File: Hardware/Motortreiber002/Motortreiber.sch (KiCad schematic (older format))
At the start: 15 parts, among them J1201 Screw_Terminal_01x04, J1202 Screw_Terminal_01x04, U1201 DRV8823

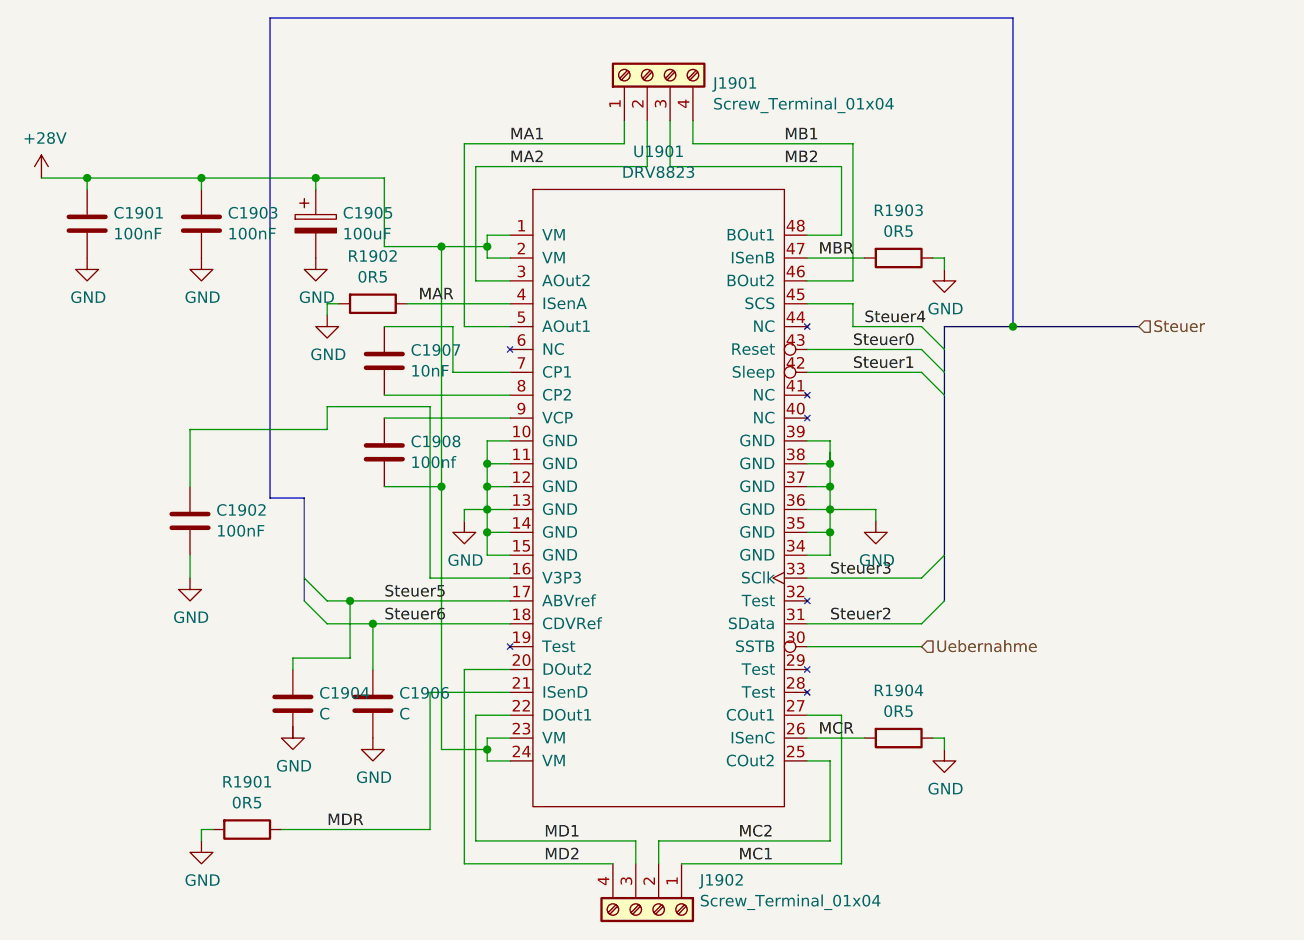
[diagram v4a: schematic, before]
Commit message: Kondensatoren auf SMD geaendert
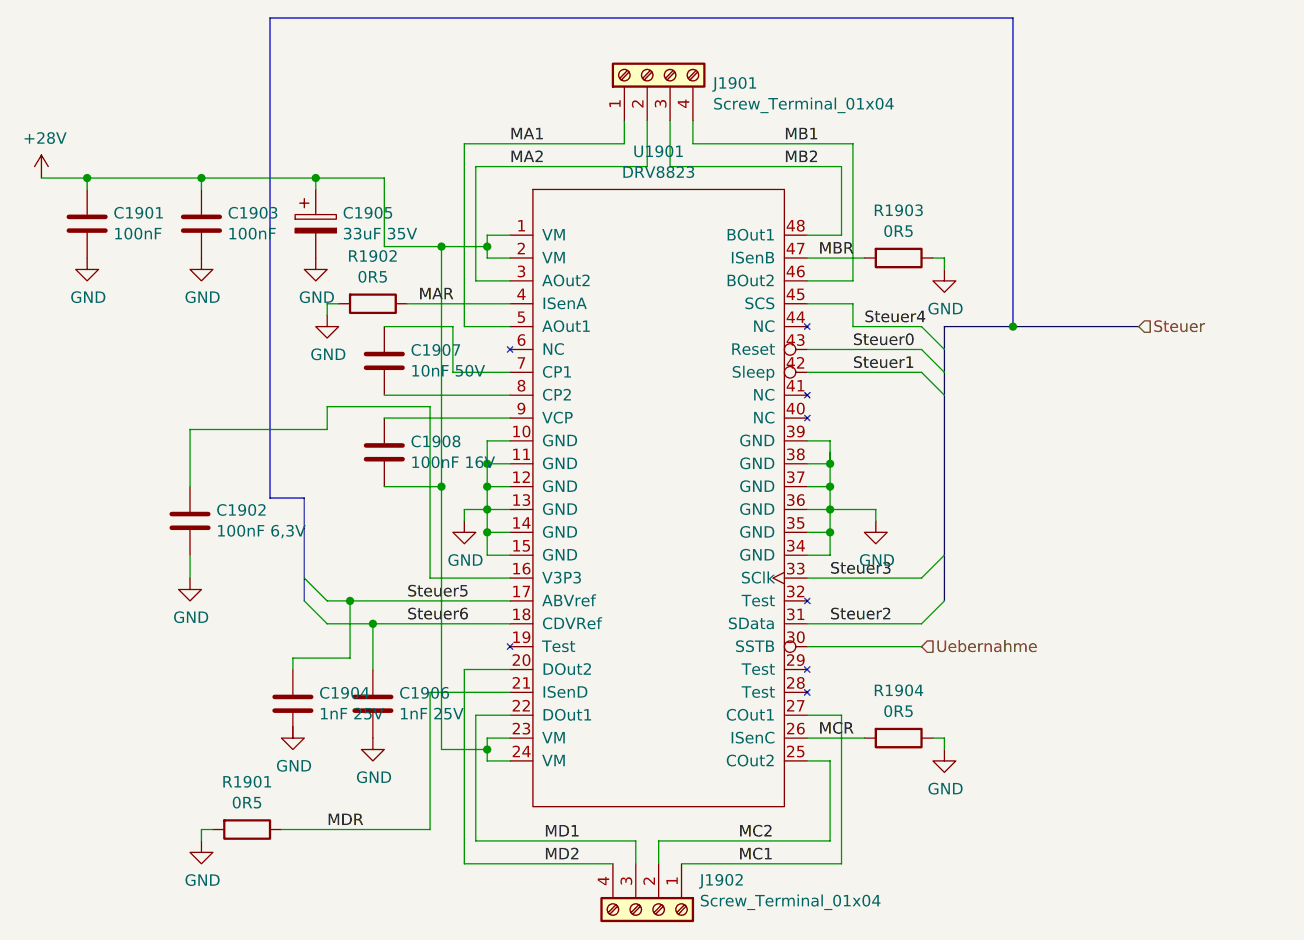
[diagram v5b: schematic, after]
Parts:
- C1201, C1203: Preis (none) -> 0,05; Reichelt (none) -> KERKO 100N
- C1202: value 100nF -> 100nF 6,3V; footprint Capacitor_SMD:C_0805_2012Metric_Pad1.15x1.40mm_HandSolder -> Capacitor_SMD:C_0201_0603Metric; Preis (none) -> 0,02; Reichelt (none) -> X5R 0201 CB 100N
- C1205: value 100uF -> 33uF 35V; footprint Capacitor_THT:CP_Radial_D8.0mm_P3.50mm -> Capacitor_THT:CP_Radial_D5.0mm_P2.00mm; Preis (none) -> 0,11; Reichelt FM-A 100U 50 -> FM-A 33U 35
- C1207: value 10nF -> 10nF 50V; footprint Capacitor_SMD:C_0805_2012Metric -> Capacitor_SMD:C_0402_1005Metric; Preis (none) -> 0,02; Reichelt (none) -> MUR GRM155R71H10
- C1208: value 100nf -> 100nF 16V; footprint Capacitor_SMD:C_0805_2012Metric_Pad1.15x1.40mm_HandSolder -> Capacitor_SMD:C_0402_1005Metric; Preis (none) -> 0,05; Reichelt (none) -> MUR GRM155R71C10
- C1404, C1406: value C -> 1nF 25V; footprint (none) -> Capacitor_SMD:C_0201_0603Metric; Preis (none) -> 0,02; Reichelt (none) -> X7R 0201 CE 1,0N
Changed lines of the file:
@@
 AR Path="/5CC752B0/5CAFBB89" Ref="#PWR?"  Part="1"
 AR Path="/5CC4B548/5CAFBB89" Ref="#PWR02101"  Part="1"
-F 0 "#PWR01901" H 1950 1900 50  0001 C CNN
+F 0 "#PWR02101" H 1950 1900 50  0001 C CNN
 F 1 "+28V" H 1965 2223 50  0000 C CNN
 F 2 "" H 2200 2100 50  0001 C CNN
@@
 AR Path="/5CC752B0/5CB597A7" Ref="#PWR?"  Part="1"
 AR Path="/5CC4B548/5CB597A7" Ref="#PWR02111"  Part="1"
-F 0 "#PWR01911" H 5600 3300 50  0001 C CNN
+F 0 "#PWR02111" H 5600 3300 50  0001 C CNN
 F 1 "GND" H 5605 3377 50  0000 C CNN
 F 2 "" H 5600 3550 50  0001 C CNN
@@
 AR Path="/5CC752B0/5CB5E84A" Ref="#PWR?"  Part="1"
 AR Path="/5CC4B548/5CB5E84A" Ref="#PWR02110"  Part="1"
-F 0 "#PWR01910" H 3800 3300 50  0001 C CNN
+F 0 "#PWR02110" H 3800 3300 50  0001 C CNN
 F 1 "GND" H 3805 3377 50  0000 C CNN
 F 2 "" H 3800 3550 50  0001 C CNN
@@
 AR Path="/5CC752B0/5CB99402" Ref="#PWR?"  Part="1"
 AR Path="/5CC4B548/5CB99402" Ref="#PWR02108"  Part="1"
-F 0 "#PWR01908" H 3200 2400 50  0001 C CNN
+F 0 "#PWR02108" H 3200 2400 50  0001 C CNN
 F 1 "GND" H 3205 2477 50  0000 C CNN
 F 2 "" H 3200 2650 50  0001 C CNN
@@
 AR Path="/5CC752B0/5CB99CB4" Ref="#PWR?"  Part="1"
 AR Path="/5CC4B548/5CB99CB4" Ref="#PWR02105"  Part="1"
-F 0 "#PWR01905" H 2650 4700 50  0001 C CNN
+F 0 "#PWR02105" H 2650 4700 50  0001 C CNN
 F 1 "GND" H 2655 4777 50  0000 C CNN
 F 2 "" H 2650 4950 50  0001 C CNN
@@
 AR Path="/5CC752B0/5CB99D3F" Ref="#PWR?"  Part="1"
 AR Path="/5CC4B548/5CB99D3F" Ref="#PWR02113"  Part="1"
-F 0 "#PWR01913" H 5900 4300 50  0001 C CNN
+F 0 "#PWR02113" H 5900 4300 50  0001 C CNN
 F 1 "GND" H 5905 4377 50  0000 C CNN
 F 2 "" H 5900 4550 50  0001 C CNN
@@
 AR Path="/5CC752B0/5CB9A10F" Ref="#PWR?"  Part="1"
 AR Path="/5CC4B548/5CB9A10F" Ref="#PWR02112"  Part="1"
-F 0 "#PWR01912" H 5900 2200 50  0001 C CNN
+F 0 "#PWR02112" H 5900 2200 50  0001 C CNN
 F 1 "GND" H 5905 2277 50  0000 C CNN
 F 2 "" H 5900 2450 50  0001 C CNN
@@
 AR Path="/5CC4B548/5CBA36F8" Ref="C2102"  Part="1"
 F 0 "C1902" H 2715 3596 50  0000 L CNN
-F 1 "100nF" H 2715 3505 50  0000 L CNN
-F 2 "Capacitor_SMD:C_0805_2012Metric_Pad1.15x1.40mm_HandSolder" H 2638 3400 50  0001 C CNN
+F 1 "100nF 6,3V" H 2715 3505 50  0000 L CNN
+F 2 "Capacitor_SMD:C_0201_0603Metric" H 2638 3400 50  0001 C CNN
 F 3 "~" H 2600 3550 50  0001 C CNN
+F 4 "X5R 0201 CB 100N" H 2600 3550 50  0001 C CNN "Reichelt"
+F 5 "0,02" H 2600 3550 50  0001 C CNN "Preis"
 	1    2600 3550
 	1    0    0    -1
@@
 AR Path="/5CC752B0/5CBA4977" Ref="#PWR?"  Part="1"
 AR Path="/5CC4B548/5CBA4977" Ref="#PWR02103"  Part="1"
-F 0 "#PWR01903" H 2600 3550 50  0001 C CNN
+F 0 "#PWR02103" H 2600 3550 50  0001 C CNN
 F 1 "GND" H 2605 3627 50  0000 C CNN
 F 2 "" H 2600 3800 50  0001 C CNN
@@
 AR Path="/5CC4B548/5CBD32BF" Ref="C2107"  Part="1"
 F 0 "C1907" H 3565 2896 50  0000 L CNN
-F 1 "10nF" H 3565 2805 50  0000 L CNN
-F 2 "Capacitor_SMD:C_0805_2012Metric" H 3488 2700 50  0001 C CNN
+F 1 "10nF 50V" H 3565 2805 50  0000 L CNN
+F 2 "Capacitor_SMD:C_0402_1005Metric" H 3488 2700 50  0001 C CNN
 F 3 "~" H 3450 2850 50  0001 C CNN
+F 4 " MUR GRM155R71H10" H 3450 2850 50  0001 C CNN "Reichelt"
+F 5 "0,02" H 3450 2850 50  0001 C CNN "Preis"
 	1    3450 2850
 	1    0    0    -1
@@
 AR Path="/5CC4B548/5CBD3B7F" Ref="C2108"  Part="1"
 F 0 "C1908" H 3565 3296 50  0000 L CNN
-F 1 "100nf" H 3565 3205 50  0000 L CNN
-F 2 "Capacitor_SMD:C_0805_2012Metric_Pad1.15x1.40mm_HandSolder" H 3488 3100 50  0001 C CNN
+F 1 "100nF 16V" H 3565 3205 50  0000 L CNN
+F 2 "Capacitor_SMD:C_0402_1005Metric" H 3488 3100 50  0001 C CNN
 F 3 "~" H 3450 3250 50  0001 C CNN
+F 4 "MUR GRM155R71C10" H 3450 3250 50  0001 C CNN "Reichelt"
+F 5 "0,05" H 3450 3250 50  0001 C CNN "Preis"
 	1    3450 3250
 	1    0    0    -1
@@
 F 2 "Capacitor_THT:C_Disc_D8.0mm_W5.0mm_P5.00mm" H 2188 2100 50  0001 C CNN
 F 3 "~" H 2150 2250 50  0001 C CNN
+F 4 "KERKO 100N" H 2150 2250 50  0001 C CNN "Reichelt"
+F 5 "0,05" H 2150 2250 50  0001 C CNN "Preis"
 	1    2150 2250
 	1    0    0    -1
@@
 F 2 "Capacitor_THT:C_Disc_D8.0mm_W5.0mm_P5.00mm" H 2688 2100 50  0001 C CNN
 F 3 "~" H 2650 2250 50  0001 C CNN
+F 4 "KERKO 100N" H 2650 2250 50  0001 C CNN "Reichelt"
+F 5 "0,05" H 2650 2250 50  0001 C CNN "Preis"
 	1    2650 2250
 	1    0    0    -1
@@
 AR Path="/5CC752B0/5CC1B08E" Ref="#PWR?"  Part="1"
 AR Path="/5CC4B548/5CC1B08E" Ref="#PWR02102"  Part="1"
-F 0 "#PWR01902" H 2150 2150 50  0001 C CNN
+F 0 "#PWR02102" H 2150 2150 50  0001 C CNN
 F 1 "GND" H 2155 2227 50  0000 C CNN
 F 2 "" H 2150 2400 50  0001 C CNN
@@
 AR Path="/5CC752B0/5CC1B34B" Ref="#PWR?"  Part="1"
 AR Path="/5CC4B548/5CC1B34B" Ref="#PWR02104"  Part="1"
-F 0 "#PWR01904" H 2650 2150 50  0001 C CNN
+F 0 "#PWR02104" H 2650 2150 50  0001 C CNN
 F 1 "GND" H 2655 2227 50  0000 C CNN
 F 2 "" H 2650 2400 50  0001 C CNN
@@
 AR Path="/5CC4B548/5CC1B722" Ref="C2105"  Part="1"
 F 0 "C1905" H 3268 2296 50  0000 L CNN
-F 1 "100uF" H 3268 2205 50  0000 L CNN
-F 2 "Capacitor_THT:CP_Radial_D8.0mm_P3.50mm" H 3188 2100 50  0001 C CNN
+F 1 "33uF 35V" H 3268 2205 50  0000 L CNN
+F 2 "Capacitor_THT:CP_Radial_D5.0mm_P2.00mm" H 3188 2100 50  0001 C CNN
 F 3 "~" H 3150 2250 50  0001 C CNN
-F 4 "FM-A 100U 50" H 3150 2250 50  0001 C CNN "Reichelt"
+F 4 "FM-A 33U 35" H 3150 2250 50  0001 C CNN "Reichelt"
+F 5 "0,11" H 3150 2250 50  0001 C CNN "Preis"
 	1    3150 2250
 	1    0    0    -1
@@
 AR Path="/5CC752B0/5CC1C247" Ref="#PWR?"  Part="1"
 AR Path="/5CC4B548/5CC1C247" Ref="#PWR02107"  Part="1"
-F 0 "#PWR01907" H 3150 2150 50  0001 C CNN
+F 0 "#PWR02107" H 3150 2150 50  0001 C CNN
 F 1 "GND" H 3155 2227 50  0000 C CNN
 F 2 "" H 3150 2400 50  0001 C CNN
@@
 AR Path="/5CC4B548/5CCBF437" Ref="C2106"  Part="1"
 F 0 "C1906" H 3515 4396 50  0000 L CNN
-F 1 "C" H 3515 4305 50  0000 L CNN
-F 2 "" H 3438 4200 50  0001 C CNN
+F 1 "1nF 25V" H 3515 4305 50  0000 L CNN
+F 2 "Capacitor_SMD:C_0201_0603Metric" H 3438 4200 50  0001 C CNN
 F 3 "~" H 3400 4350 50  0001 C CNN
+F 4 "X7R 0201 CE 1,0N" H 3400 4350 50  0001 C CNN "Reichelt"
+F 5 "0,02" H 3400 4350 50  0001 C CNN "Preis"
 	1    3400 4350
 	1    0    0    -1
@@
 AR Path="/5CC4B548/5CCBF8F9" Ref="C2104"  Part="1"
 F 0 "C1904" H 3165 4396 50  0000 L CNN
-F 1 "C" H 3165 4305 50  0000 L CNN
-F 2 "" H 3088 4200 50  0001 C CNN
+F 1 "1nF 25V" H 3165 4305 50  0000 L CNN
+F 2 "Capacitor_SMD:C_0201_0603Metric" H 3088 4200 50  0001 C CNN
 F 3 "~" H 3050 4350 50  0001 C CNN
+F 4 "X7R 0201 CE 1,0N" H 3050 4350 50  0001 C CNN "Reichelt"
+F 5 "0,02" H 3050 4350 50  0001 C CNN "Preis"
 	1    3050 4350
 	1    0    0    -1
@@
 AR Path="/5CC7522D/5CCBFD0C" Ref="#PWR02209"  Part="1"
 AR Path="/5CC4B548/5CCBFD0C" Ref="#PWR02109"  Part="1"
-F 0 "#PWR01909" H 3400 4250 50  0001 C CNN
+F 0 "#PWR02109" H 3400 4250 50  0001 C CNN
 F 1 "GND" H 3405 4327 50  0000 C CNN
 F 2 "" H 3400 4500 50  0001 C CNN
@@
 AR Path="/5CC7522D/5CCBFDA5" Ref="#PWR02206"  Part="1"
 AR Path="/5CC4B548/5CCBFDA5" Ref="#PWR02106"  Part="1"
-F 0 "#PWR01906" H 3050 4200 50  0001 C CNN
+F 0 "#PWR02106" H 3050 4200 50  0001 C CNN
 F 1 "GND" H 3055 4277 50  0000 C CNN
 F 2 "" H 3050 4450 50  0001 C CNN
@@
 Text Label 5400 4000 0    50   ~ 0
 Steuer2
-Text Label 3450 3900 0    50   ~ 0
+Text Label 3550 3900 0    50   ~ 0
 Steuer5
-Text Label 3450 4000 0    50   ~ 0
+Text Label 3550 4000 0    50   ~ 0
 Steuer6
 Entry Wire Line
@@
 Text HLabel 5800 4100 2    50   Input ~ 0
 Uebernahme
-Wire Bus Line
-	3100 3450 3100 3900
-Wire Bus Line
-	5900 2700 5900 3900
 Text Label 3600 2600 0    50   ~ 0
 MAR
@@
 Text Label 5350 4500 0    50   ~ 0
 MCR
+Wire Bus Line
+	3100 3450 3100 3900
+Wire Bus Line
+	5900 2700 5900 3900
 $EndSCHEMATC

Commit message: weiteres routing
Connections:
- net GND: now also C1404.2
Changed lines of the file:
@@
 AR Path="/5CC752B0/5CAFBB89" Ref="#PWR?"  Part="1"
 AR Path="/5CC4B548/5CAFBB89" Ref="#PWR02101"  Part="1"
-F 0 "#PWR02101" H 1950 1900 50  0001 C CNN
+F 0 "#PWR01901" H 1950 1900 50  0001 C CNN
 F 1 "+28V" H 1965 2223 50  0000 C CNN
 F 2 "" H 2200 2100 50  0001 C CNN
@@
 AR Path="/5CC752B0/5CB597A7" Ref="#PWR?"  Part="1"
 AR Path="/5CC4B548/5CB597A7" Ref="#PWR02111"  Part="1"
-F 0 "#PWR02111" H 5600 3300 50  0001 C CNN
+F 0 "#PWR01911" H 5600 3300 50  0001 C CNN
 F 1 "GND" H 5605 3377 50  0000 C CNN
 F 2 "" H 5600 3550 50  0001 C CNN
@@
 AR Path="/5CC752B0/5CB5E84A" Ref="#PWR?"  Part="1"
 AR Path="/5CC4B548/5CB5E84A" Ref="#PWR02110"  Part="1"
-F 0 "#PWR02110" H 3800 3300 50  0001 C CNN
+F 0 "#PWR01910" H 3800 3300 50  0001 C CNN
 F 1 "GND" H 3805 3377 50  0000 C CNN
 F 2 "" H 3800 3550 50  0001 C CNN
@@
 AR Path="/5CC752B0/5CB99402" Ref="#PWR?"  Part="1"
 AR Path="/5CC4B548/5CB99402" Ref="#PWR02108"  Part="1"
-F 0 "#PWR02108" H 3200 2400 50  0001 C CNN
+F 0 "#PWR01908" H 3200 2400 50  0001 C CNN
 F 1 "GND" H 3205 2477 50  0000 C CNN
 F 2 "" H 3200 2650 50  0001 C CNN
@@
 AR Path="/5CC752B0/5CB99CB4" Ref="#PWR?"  Part="1"
 AR Path="/5CC4B548/5CB99CB4" Ref="#PWR02105"  Part="1"
-F 0 "#PWR02105" H 2650 4700 50  0001 C CNN
+F 0 "#PWR01905" H 2650 4700 50  0001 C CNN
 F 1 "GND" H 2655 4777 50  0000 C CNN
 F 2 "" H 2650 4950 50  0001 C CNN
@@
 AR Path="/5CC752B0/5CB99D3F" Ref="#PWR?"  Part="1"
 AR Path="/5CC4B548/5CB99D3F" Ref="#PWR02113"  Part="1"
-F 0 "#PWR02113" H 5900 4300 50  0001 C CNN
+F 0 "#PWR01913" H 5900 4300 50  0001 C CNN
 F 1 "GND" H 5905 4377 50  0000 C CNN
 F 2 "" H 5900 4550 50  0001 C CNN
@@
 AR Path="/5CC752B0/5CB9A10F" Ref="#PWR?"  Part="1"
 AR Path="/5CC4B548/5CB9A10F" Ref="#PWR02112"  Part="1"
-F 0 "#PWR02112" H 5900 2200 50  0001 C CNN
+F 0 "#PWR01912" H 5900 2200 50  0001 C CNN
 F 1 "GND" H 5905 2277 50  0000 C CNN
 F 2 "" H 5900 2450 50  0001 C CNN
@@
 AR Path="/5CC752B0/5CBA4977" Ref="#PWR?"  Part="1"
 AR Path="/5CC4B548/5CBA4977" Ref="#PWR02103"  Part="1"
-F 0 "#PWR02103" H 2600 3550 50  0001 C CNN
+F 0 "#PWR01903" H 2600 3550 50  0001 C CNN
 F 1 "GND" H 2605 3627 50  0000 C CNN
 F 2 "" H 2600 3800 50  0001 C CNN
@@
 AR Path="/5CC752B0/5CC1B08E" Ref="#PWR?"  Part="1"
 AR Path="/5CC4B548/5CC1B08E" Ref="#PWR02102"  Part="1"
-F 0 "#PWR02102" H 2150 2150 50  0001 C CNN
+F 0 "#PWR01902" H 2150 2150 50  0001 C CNN
 F 1 "GND" H 2155 2227 50  0000 C CNN
 F 2 "" H 2150 2400 50  0001 C CNN
@@
 AR Path="/5CC752B0/5CC1B34B" Ref="#PWR?"  Part="1"
 AR Path="/5CC4B548/5CC1B34B" Ref="#PWR02104"  Part="1"
-F 0 "#PWR02104" H 2650 2150 50  0001 C CNN
+F 0 "#PWR01904" H 2650 2150 50  0001 C CNN
 F 1 "GND" H 2655 2227 50  0000 C CNN
 F 2 "" H 2650 2400 50  0001 C CNN
@@
 AR Path="/5CC752B0/5CC1C247" Ref="#PWR?"  Part="1"
 AR Path="/5CC4B548/5CC1C247" Ref="#PWR02107"  Part="1"
-F 0 "#PWR02107" H 3150 2150 50  0001 C CNN
+F 0 "#PWR01907" H 3150 2150 50  0001 C CNN
 F 1 "GND" H 3155 2227 50  0000 C CNN
 F 2 "" H 3150 2400 50  0001 C CNN
@@
 AR Path="/5CC7522D/5CCBFD0C" Ref="#PWR02209"  Part="1"
 AR Path="/5CC4B548/5CCBFD0C" Ref="#PWR02109"  Part="1"
-F 0 "#PWR02109" H 3400 4250 50  0001 C CNN
+F 0 "#PWR01909" H 3400 4250 50  0001 C CNN
 F 1 "GND" H 3405 4327 50  0000 C CNN
 F 2 "" H 3400 4500 50  0001 C CNN
@@
 L power:GND #PWR01406
 U 1 1 5CCBFDA5
-P 3050 4450
+P 3050 4500
 AR Path="/5CB48D70/5CCBFDA5" Ref="#PWR01406"  Part="1"
 AR Path="/5CB4900E/5CCBFDA5" Ref="#PWR01519"  Part="1"
@@
 AR Path="/5CC7522D/5CCBFDA5" Ref="#PWR02206"  Part="1"
 AR Path="/5CC4B548/5CCBFDA5" Ref="#PWR02106"  Part="1"
-F 0 "#PWR02106" H 3050 4200 50  0001 C CNN
-F 1 "GND" H 3055 4277 50  0000 C CNN
-F 2 "" H 3050 4450 50  0001 C CNN
-F 3 "" H 3050 4450 50  0001 C CNN
-	1    3050 4450
-	1    0    0    -1
-$EndComp
+F 0 "#PWR01906" H 3050 4250 50  0001 C CNN
+F 1 "GND" H 3055 4327 50  0000 C CNN
+F 2 "" H 3050 4500 50  0001 C CNN
+F 3 "" H 3050 4500 50  0001 C CNN
+	1    3050 4500
+	1    0    0    -1
+$EndComp
